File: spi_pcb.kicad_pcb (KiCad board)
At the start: 2 copper layers, 65 x 56 mm, 6 parts, among them J1 GPIO, U1 LMZ23605TZ

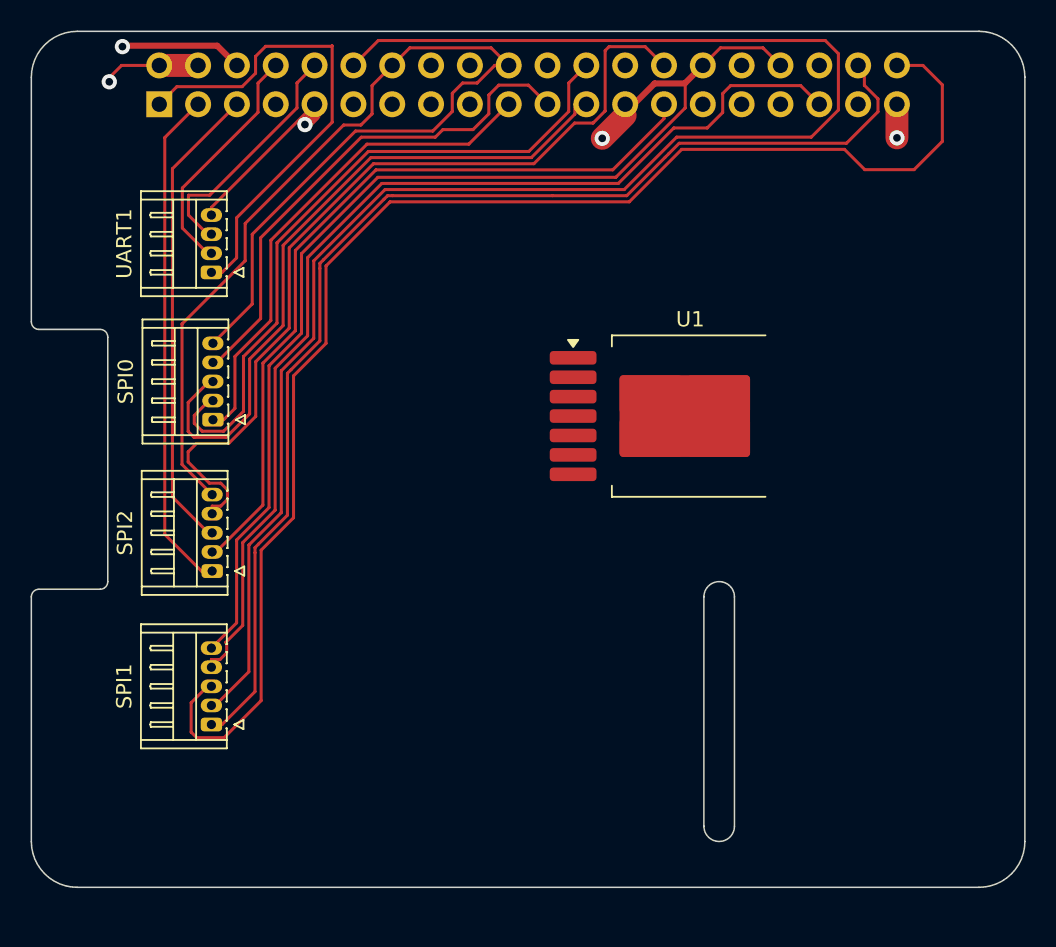
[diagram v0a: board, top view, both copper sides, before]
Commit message: Sent connectors to back plane
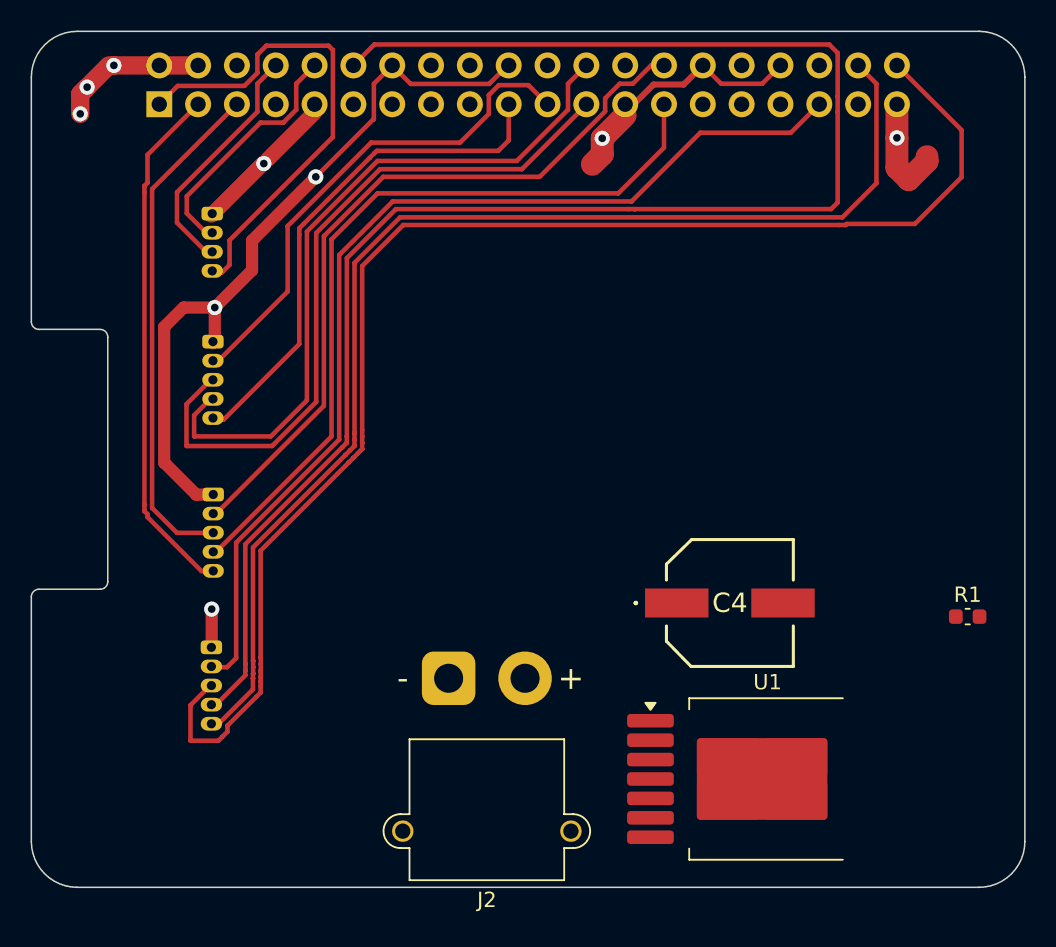
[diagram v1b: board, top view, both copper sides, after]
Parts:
- added C4: 50SVPF39M, Kicad Library:16SVPT560M, F.Cu at (145.7, 81.4)
- added J2: PWR, Connector_AMASS:AMASS_XT30PW-M_1x02_P2.50mm_Horizontal, F.Cu at (127.3, 86.3)
- added R1: 5.62k, Capacitor_SMD:C_0603_1608Metric, F.Cu at (161.3, 82.3)
- SPI0, SPI1, SPI2, UART1: moved to B.Cu
- moved U1 24.3 mm to (148.2, 92.9)
- moved SPI0 5.11 mm to (111.9, 64.3), turned to -90 degrees
- moved SPI1 5.05 mm to (111.8, 84.3), turned to -90 degrees
- moved SPI2 5.01 mm to (111.9, 74.3), turned to -90 degrees
- moved UART1 3.85 mm to (111.8, 55.9), turned to -90 degrees
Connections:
- U1 pad 7: Net-(U1-VOUT) -> +5V
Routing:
- net GND: track 170.0 -> 82.5 mm, vias 4 -> 5
- net /ID_SCL: track 56.4 -> 48.7 mm
- net +5V: track 5.91 -> 10.4 mm, vias 1 -> 3
- net /GPIO20/PCM.DIN: track 77.7 -> 81.4 mm, vias 0 -> 1
- net /GPIO19/PCM.FS: track 69.2 -> 66.5 mm
- net /GPIO3/SCL1: track 31.0 -> 33.3 mm
- net /GPIO11/SPI0.SCLK: track 45.2 -> 47.3 mm
- net /GPIO18/PCM.CLK: track 107.1 -> 109.2 mm
- net /GPIO8/SPI0.CE0: track 45.1 -> 47.1 mm
- net /GPIO2/SDA1: track 33.1 -> 34.2 mm
- net /GPIO10/SPI0.MOSI: track 33.0 -> 33.7 mm
- net /GPIO9/SPI0.MISO: track 34.0 -> 33.4 mm
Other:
- outline, holes or cut-outs redrawn
- board text removed: "CAMERA (OPTIONAL)"

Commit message: V0
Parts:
- added C1: EEF-CX0J221R, Kicad Library:EEFCX0J101R, F.Cu at (119.9, 83.3)
- added C2: C3216X5R0J107M160AB, Kicad Library:CAPC3216X180N, F.Cu at (124.4, 82.7)
- added R2: 1.05k, Resistor_SMD:R_0603_1608Metric, F.Cu at (130.5, 83.8)
- J2: moved to B.Cu
- R1: footprint Capacitor_SMD:C_0603_1608Metric -> Resistor_SMD:R_0603_1608Metric
- moved R1 34.1 mm to (127.2, 83.8)
- moved J2 27.9 mm to (155.1, 88.6), turned to 0 degrees
- moved U1 19.2 mm to (129.1, 94.8), turned to -90 degrees
- moved C4 12.4 mm to (139.7, 92.3), turned to -90 degrees
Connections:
- SPI0 pad 1: /GPIO10/SPI0.MOSI -> GND
- SPI0 pad 2: /GPIO8/SPI0.CE0 -> /GPIO9/SPI0.MISO
- SPI0 pad 4: /GPIO9/SPI0.MISO -> /GPIO8/SPI0.CE0
- SPI0 pad 5: GND -> /GPIO10/SPI0.MOSI
- SPI1 pad 1: /GPIO20/PCM.DIN -> GND
- SPI1 pad 2: /GPIO18/PCM.CLK -> /GPIO19/PCM.FS
- SPI1 pad 4: /GPIO19/PCM.FS -> /GPIO18/PCM.CLK
- SPI1 pad 5: GND -> /GPIO20/PCM.DIN
- SPI2 pad 1: /GPIO2/SDA1 -> GND
- SPI2 pad 2: /ID_SDA -> /ID_SCL
- SPI2 pad 4: /ID_SCL -> /ID_SDA
- SPI2 pad 5: GND -> /GPIO2/SDA1
- UART1 pad 1: +3V3 -> GND
- UART1 pad 2: /GPIO14/TXD0 -> /GPIO15/RXD0
- UART1 pad 3: /GPIO15/RXD0 -> /GPIO14/TXD0
- UART1 pad 4: GND -> +3V3
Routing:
- net GND: track 82.5 -> 117.8 mm, vias 5 -> 12
- net Net-(C4-+): track 0.00 -> 7.51 mm
- net Net-(U1-FB): track 0.00 -> 7.36 mm
- net /ID_SDA: track 50.9 -> 58.1 mm
- net /GPIO20/PCM.DIN: track 81.4 -> 77.7 mm, vias 1 -> 0
- net /GPIO10/SPI0.MOSI: track 33.7 -> 37.1 mm
- net /GPIO19/PCM.FS: track 66.5 -> 69.7 mm
- net /GPIO3/SCL1: track 33.3 -> 31.8 mm
- net /GPIO21/PCM.DOUT: track 91.7 -> 90.5 mm
- net /GPIO11/SPI0.SCLK: track 47.3 -> 48.3 mm
- net /ID_SCL: track 48.7 -> 49.7 mm
- net /GPIO8/SPI0.CE0: track 47.1 -> 48.1 mm
- net /GPIO2/SDA1: track 34.2 -> 33.7 mm
- net +5V: vias 3 -> 7
- added copper zone on F.Cu, net (none)
- added copper zone on B.Cu, net +5V
- added copper zone on F.Cu, net +5V
- added copper zone on B.Cu, net GND
- added copper zone on F.Cu, net GND
- added copper zone on F.Cu, net Net-(C4-+)

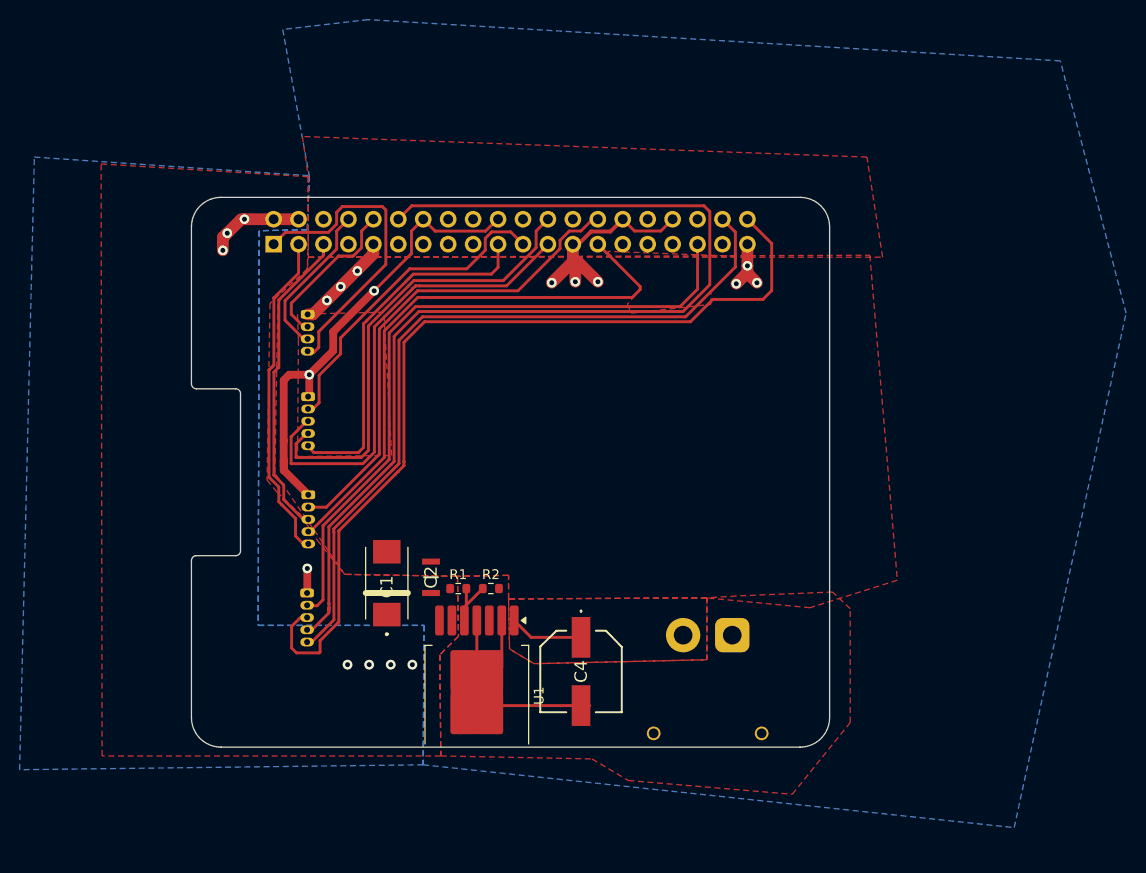
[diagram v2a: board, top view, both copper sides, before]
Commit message: Add copper pours, cooling cutout and correct vias.
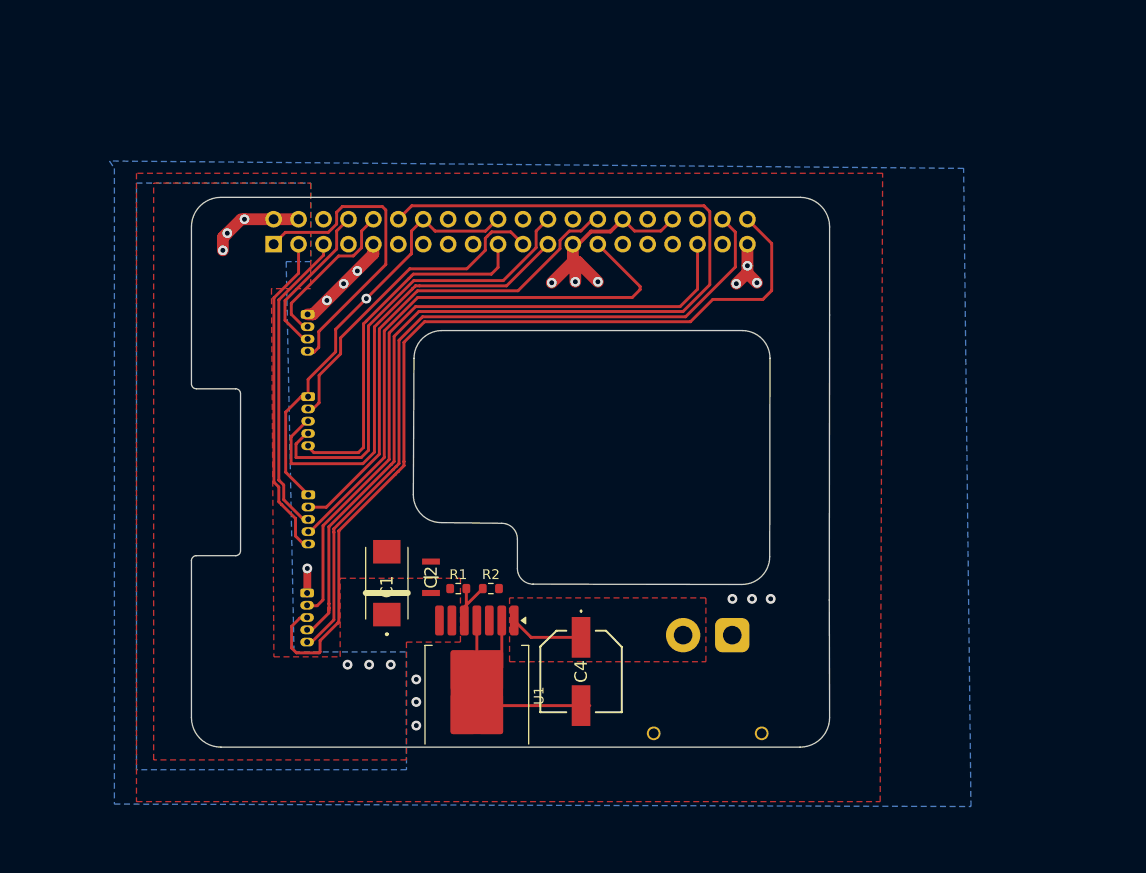
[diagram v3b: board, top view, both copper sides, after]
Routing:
- net GND: track 117.8 -> 113.7 mm, vias 12 -> 17
- net +5V: vias 7 -> 6
- removed copper zone on F.Cu, net (none)
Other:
- outline, holes or cut-outs redrawn

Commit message: Added VCC ceramic filter caps
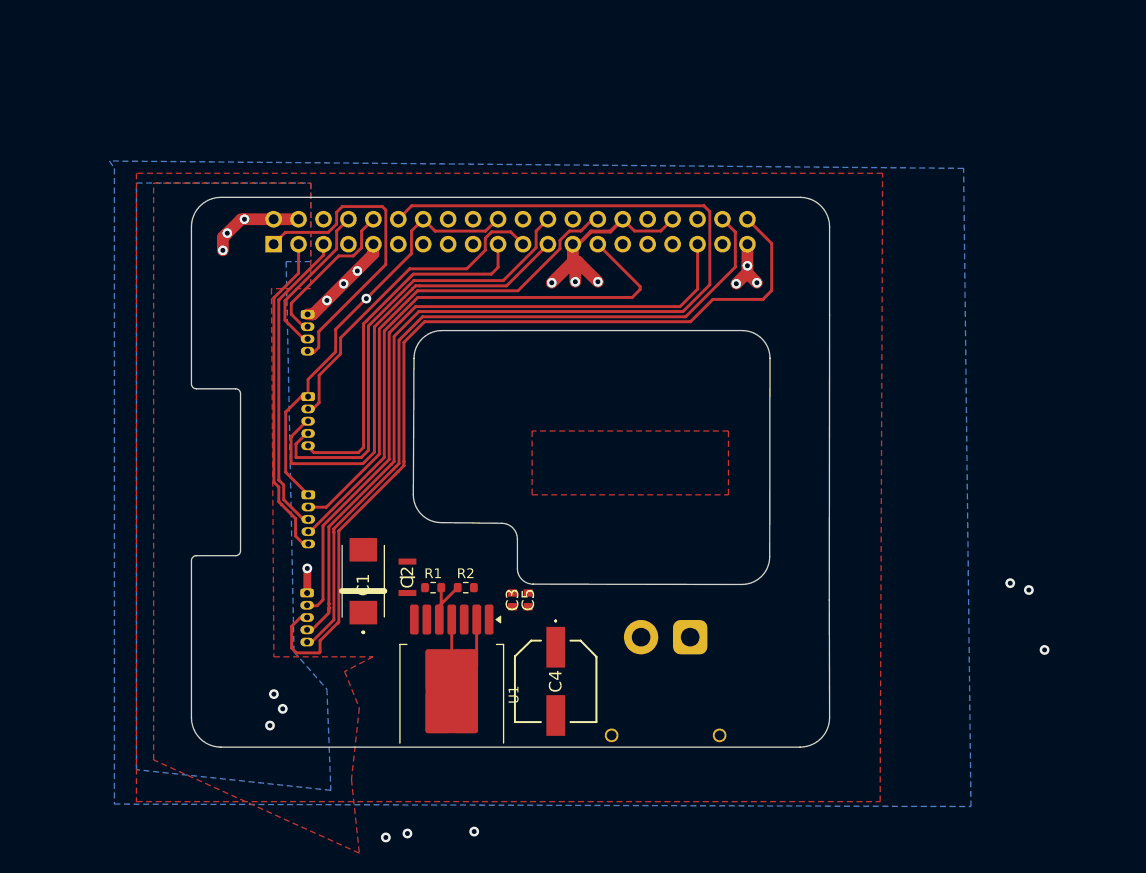
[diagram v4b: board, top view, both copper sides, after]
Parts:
- added C3: 2.2uF, Kicad Library:CAPC1608X90N, F.Cu at (132.7, 85.0)
- added C5: 2.2uF, Kicad Library:CAPC1608X90N, F.Cu at (134.3, 85.0)
- C4: value 50SVPF39M -> 39uF
- R1: value 5.62k -> 5.6k
- moved J2 4.29 mm to (150.8, 88.8)
- moved C4 2.77 mm to (137.1, 93.3)
- moved R2 2.56 mm to (127.9, 83.8)
- moved R1 2.56 mm to (124.6, 83.8)
- moved U1 2.56 mm to (126.5, 94.7)
- moved C1 2.41 mm to (117.5, 83.1)
- moved C2 2.40 mm to (122.0, 82.7)
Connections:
- J1 pad 17: +3V3 -> unconnected-(J1-Pin_17-Pad17)
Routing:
- net GND: track 113.7 -> 103.5 mm
- net Net-(C4-+): track 7.51 -> 0.00 mm

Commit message: Rerouted for 0.25mm copper clearance. Added sample SPI impedance matching resistor.
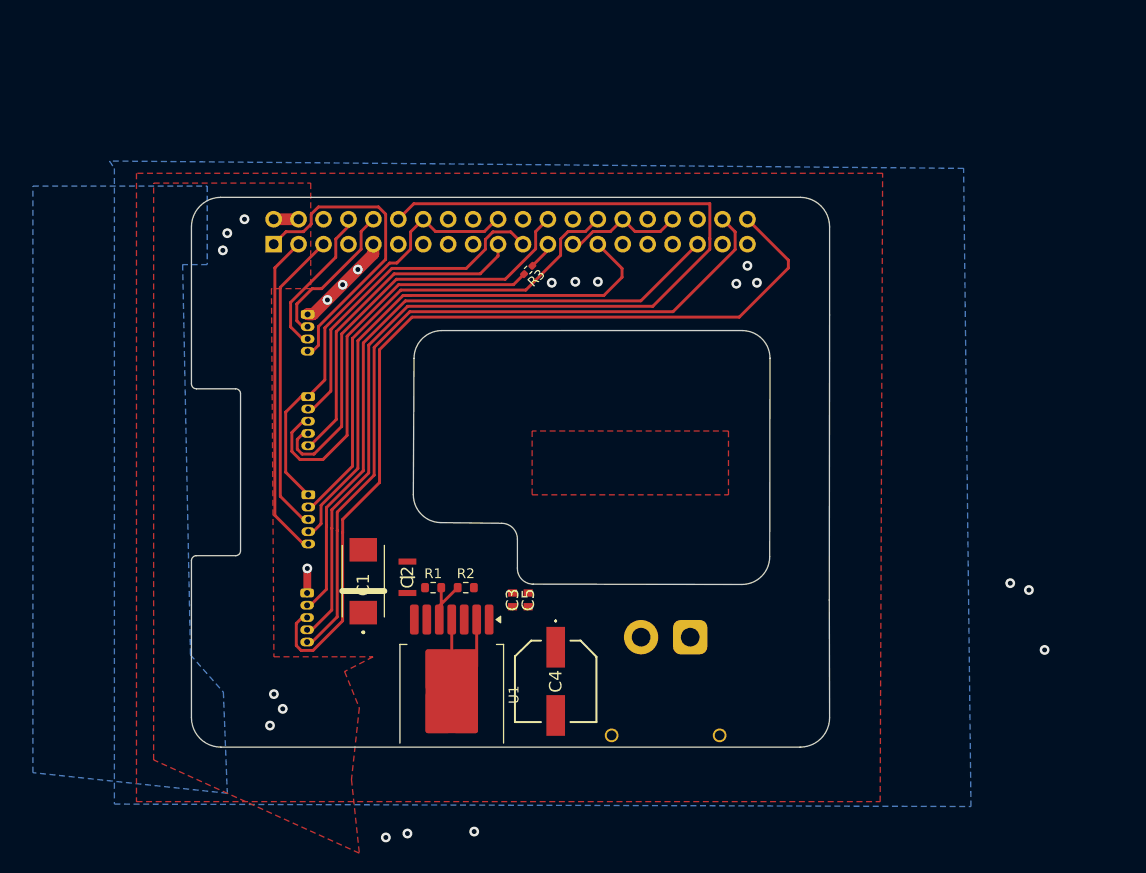
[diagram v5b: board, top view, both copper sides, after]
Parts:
- added R3: 10, Resistor_SMD:R_0402_1005Metric_Pad0.72x0.64mm_HandSolder, F.Cu at (134.3, 51.4)
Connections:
- SPI0 pad 3: /GPIO11/SPI0.SCLK -> Net-(SPI0-Pin_3)
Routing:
- net /GPIO11/SPI0.SCLK: track 48.3 -> 2.87 mm
- net Net-(SPI0-Pin_3): track 0.00 -> 42.0 mm
- net GND: track 103.5 -> 88.2 mm, vias 17 -> 16
- net +5V: track 10.4 -> 2.54 mm
- net /GPIO10/SPI0.MOSI: track 37.1 -> 33.8 mm
- net /GPIO8/SPI0.CE0: track 48.1 -> 45.5 mm
- net /GPIO19/PCM.FS: track 69.7 -> 67.5 mm
- net /GPIO9/SPI0.MISO: track 33.2 -> 34.1 mm
- net /ID_SDA: track 58.1 -> 57.3 mm
- net /GPIO18/PCM.CLK: track 109.0 -> 108.2 mm
- net /GPIO15/RXD0: track 16.7 -> 16.0 mm
- net +3V3: track 32.1 -> 31.4 mm
- net /ID_SCL: track 49.7 -> 50.2 mm

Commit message: Cut cooling hole for Raspberry CPU, redone vias. Added 10 Ohm impedance matching for source SPI signals.
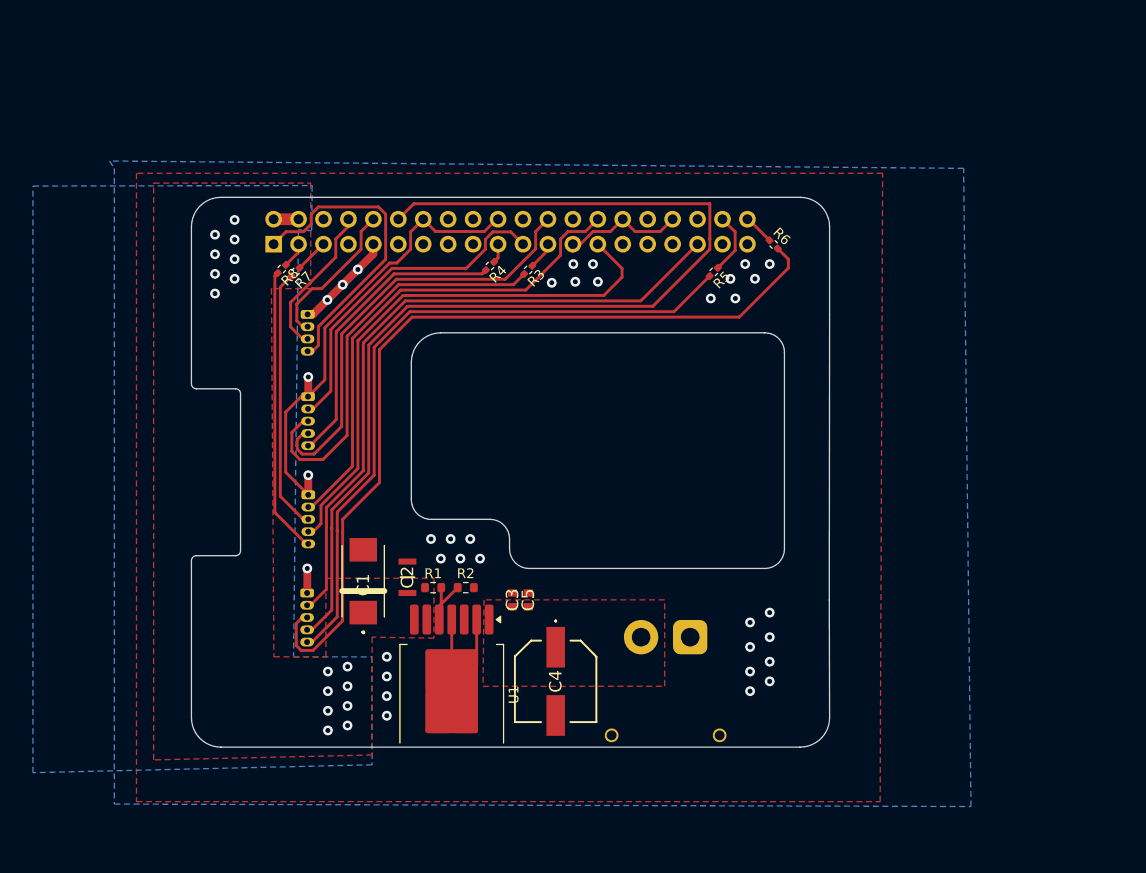
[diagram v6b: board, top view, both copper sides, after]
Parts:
- added R4: 10, Resistor_SMD:R_0402_1005Metric_Pad0.72x0.64mm_HandSolder, F.Cu at (130.4, 51.0)
- added R5: 10, Resistor_SMD:R_0402_1005Metric_Pad0.72x0.64mm_HandSolder, F.Cu at (153.2, 51.6)
- added R6: 10, Resistor_SMD:R_0402_1005Metric_Pad0.72x0.64mm_HandSolder, F.Cu at (159.3, 48.8)
- added R7: 10, Resistor_SMD:R_0402_1005Metric_Pad0.72x0.64mm_HandSolder, F.Cu at (110.6, 51.6)
- added R8: 10, Resistor_SMD:R_0402_1005Metric_Pad0.72x0.64mm_HandSolder, F.Cu at (109.2, 51.3)
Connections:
- SPI0 pad 5: /GPIO10/SPI0.MOSI -> Net-(SPI0-Pin_5)
- SPI1 pad 3: /GPIO21/PCM.DOUT -> Net-(SPI1-Pin_3)
- SPI1 pad 5: /GPIO20/PCM.DIN -> Net-(SPI1-Pin_5)
- SPI2 pad 3: /GPIO3/SCL1 -> Net-(SPI2-Pin_3)
- SPI2 pad 5: /GPIO2/SDA1 -> Net-(SPI2-Pin_5)
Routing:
- net /GPIO21/PCM.DOUT: track 90.7 -> 3.14 mm
- net Net-(SPI1-Pin_3): track 0.00 -> 86.5 mm
- net /GPIO20/PCM.DIN: track 77.7 -> 6.21 mm
- net Net-(SPI1-Pin_5): track 0.00 -> 70.3 mm
- net /GPIO10/SPI0.MOSI: track 33.8 -> 1.98 mm
- net Net-(SPI0-Pin_5): track 0.00 -> 30.7 mm
- net /GPIO2/SDA1: track 33.2 -> 2.64 mm
- net Net-(SPI2-Pin_5): track 0.00 -> 29.2 mm
- net /GPIO3/SCL1: track 31.3 -> 3.42 mm
- net Net-(SPI2-Pin_3): track 0.00 -> 26.7 mm
- net GND: track 88.2 -> 91.7 mm, vias 16 -> 35
- net +5V: vias 6 -> 16
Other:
- outline, holes or cut-outs redrawn
